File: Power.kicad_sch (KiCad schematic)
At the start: 18 parts, among them U5 IRS2186, U6 IRS2186, U7 IRS2186

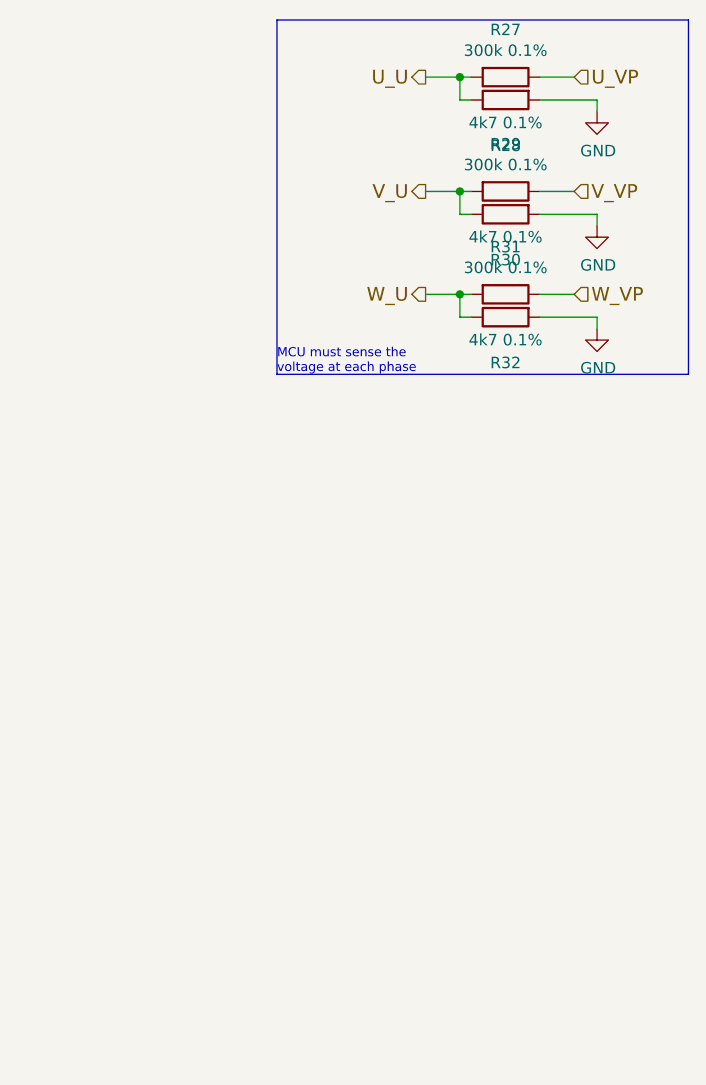
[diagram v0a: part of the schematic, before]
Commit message: HSWR V4.1: - added opamp for better voltage measurement
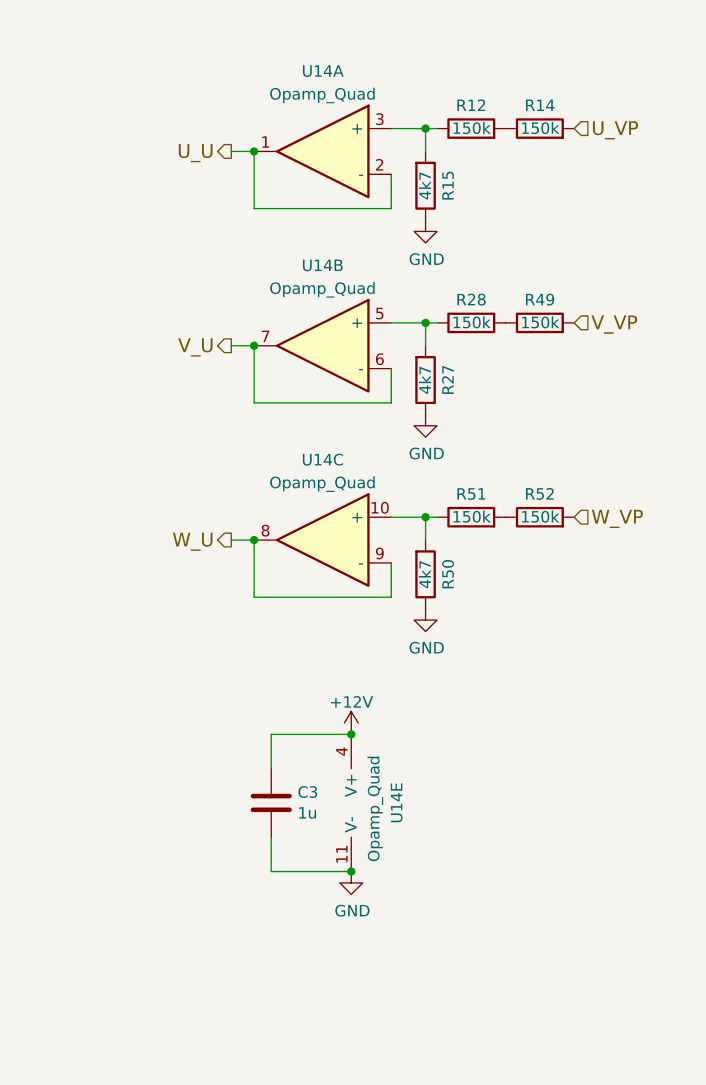
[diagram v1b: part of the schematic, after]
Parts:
- removed R29, R31: 300k 0.1%, Resistor_SMD:R_0805_2012Metric, symbol Device:R
- removed R30, R32: 4k7 0.1%, Resistor_SMD:R_0805_2012Metric, symbol Device:R
- added C3: 1u, Capacitor_SMD:C_0805_2012Metric, symbol Device:C
- added R12, R14, R49, R51, R52: 150k, Resistor_SMD:R_0805_2012Metric, symbol Device:R
- added R15, R50: 4k7, Resistor_SMD:R_0805_2012Metric, symbol Device:R
- added U14: Opamp_Quad, Package_SO:SO-14_3.9x8.65mm_P1.27mm, symbol Device:Opamp_Quad
- R27: value 300k 0.1% -> 4k7
- R28: value 4k7 0.1% -> 150k
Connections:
- net +12V: now also C3.1, U14.4 (V+)
- net GND: now also R27.1, C3.2, R15.1, R50.1, U14.11 (V-); no longer R28.2
- net U_U: now also U14.1, U14.2 (-); no longer R27.2, R28.1
- net U_VP: now also R14.2; no longer R27.1
- net V_U: now also U14.6 (-), U14.7
- net V_VP: now also R49.2
- net W_U: now also U14.8, U14.9 (-)
- net W_VP: now also R52.2
- new net: R50.2, R51.1, U14.10 (+)
- new net: R12.1, R15.2, U14.3 (+)
- new net: R12.2, R14.1
- new net: R27.2, R28.1, U14.5 (+)
- new net: R51.2, R52.1
- new net: R28.2, R49.1
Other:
- note removed: "MCU must sense the voltage at each phase"
